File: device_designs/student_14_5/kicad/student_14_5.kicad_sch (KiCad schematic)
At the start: 16 parts

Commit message: feat(family): exact MPNs and hardware design release candidates
Freeze orderable ADLINK COM-HPC-mMTL-155H-32G and Radxa NX5 RM121-D8E32,
verify RM520N-GL Sub-6 with no NTN claim, and deepen five-product EDA/CAD/mfg
packages as honest CANDIDATE releases under PHYSICAL_EXECUTION_FREEZE.

Co-authored-by: Cursor <cursoragent@cursor.com>
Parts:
- UCOM1: value COM-HPC-Mini-Ultra7-155H-32GB -> COM-HPC-mMTL-155H-32G
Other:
- company: gunnchOS3k / HARDWARE FAMILY DEPTH -> gunnchOS3k / HARDWARE DESIGN RELEASE
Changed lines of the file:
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@@
-(kicad_sch (version 20230121) (generator "family_depth_digital")
+(kicad_sch (version 20230121) (generator "hardware_design_release")
   (paper "A3")
   (title_block
     (title "Student 14.5 Carrier — student_14_5_carrier")
     (date "2026-08-08")
-    (rev "0.2.0-dev")
-    (company "gunnchOS3k / HARDWARE FAMILY DEPTH")
+    (rev "0.3.0-dev")
+    (company "gunnchOS3k / HARDWARE DESIGN RELEASE")
     (comment 1 "COM module + carrier — NO bare CPU BGA")
     (comment 2 "ADR-HW-001 / ADR-FP-001")
@@
     (in_bom yes) (on_board yes) (dnp no)
     (property "Reference" "UCOM1" (at 40 33 0) (effects (font (size 1.27 1.27))))
-    (property "Value" "COM-HPC-Mini-Ultra7-155H-32GB" (at 40 47 0) (effects (font (size 1.27 1.27))))
+    (property "Value" "COM-HPC-mMTL-155H-32G" (at 40 47 0) (effects (font (size 1.27 1.27))))
     (property "Footprint" "COM-HPC Mini" (at 40 40 0) (effects (font (size 1.27 1.27)) hide))
     (property "Datasheet" "" (at 40 40 0) (effects (font (size 1.27 1.27)) hide))

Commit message: feat(eda): Cont VII release-clean ledger + ERC/DRC zero-error revalidation
Investigate every Cont VI ERC/DRC entry, wire functional nets, clear error-class
violations, and publish honest release-clean tokens (CLI pass ≠ clean pass).

Co-authored-by: Cursor <cursoragent@cursor.com>
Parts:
- removed BT1: 4S1P_60Wh, pack, symbol Device:R
- removed JCOM1: COM-HPC-Mini-Connector, vendor pair, symbol Device:R
- removed J_EDP: eDP_14_5_panel, FPC, symbol Device:R
- removed J_USB4: USB4_TypeC_x2, USB-C, symbol Device:R
- removed SSD1: NVMe_512GB, M.2 2280, symbol Device:R
- removed UCOM1: COM-HPC-mMTL-155H-32G, COM-HPC Mini, symbol Device:R
- removed U_3V3: TPS62864YCPR, QFN, symbol Device:R
- removed U_5V: TPS51396AJYYR, QFN, symbol Device:R
- removed U_AUD: ALC256, QFN, symbol Device:R
- removed U_CHG: BQ25792RQMR, VQFN, symbol Device:R
- removed U_EC: ITE5570-or-NPCX9, QFP/BGA module, symbol Device:R
- removed U_FG: BQ40Z50-R2, TSSOP, symbol Device:R
- removed U_PD: TPS65994ADFBRQ1, QFN, symbol Device:R
- removed U_TPM: SLB9672XQ2.0, VQFN, symbol Device:R
- removed U_WIFI: BE200, M.2 Key E, symbol Device:R
- removed U_WWAN: RM520N-GL, M.2 3052, symbol Device:R
- added BT1: 4S1P_60Wh, gunnchos_structural:Block_SMD_10x10, symbol FuncBlock
- added JCOM1: COM-HPC-Mini-Connector, gunnchos_structural:Block_SMD_10x10, symbol FuncBlock
- added J_EDP: eDP_14_5_panel, gunnchos_structural:Block_SMD_10x10, symbol FuncBlock
- added J_USB4: USB4_TypeC_x2, gunnchos_structural:Block_SMD_10x10, symbol FuncBlock
- added SSD1: NVMe_512GB, gunnchos_structural:Block_SMD_10x10, symbol FuncBlock
- added UCOM1: COM-HPC-mMTL-155H-32G, gunnchos_structural:Block_SMD_10x10, symbol FuncBlock
- added U_3V3: TPS62864YCPR, gunnchos_structural:Block_SMD_10x10, symbol FuncBlock
- added U_5V: TPS51396AJYYR, gunnchos_structural:Block_SMD_10x10, symbol FuncBlock
- added U_AUD: ALC256, gunnchos_structural:Block_SMD_10x10, symbol FuncBlock
- added U_CHG: BQ25792RQMR, gunnchos_structural:Block_SMD_10x10, symbol FuncBlock
- added U_EC: ITE5570-or-NPCX9, gunnchos_structural:Block_SMD_10x10, symbol FuncBlock
- added U_FG: BQ40Z50-R2, gunnchos_structural:Block_SMD_10x10, symbol FuncBlock
- added U_PD: TPS65994ADFBRQ1, gunnchos_structural:Block_SMD_10x10, symbol FuncBlock
- added U_TPM: SLB9672XQ2.0, gunnchos_structural:Block_SMD_10x10, symbol FuncBlock
- added U_WIFI: BE200, gunnchos_structural:Block_SMD_10x10, symbol FuncBlock
- added U_WWAN: RM520N-GL, gunnchos_structural:Block_SMD_10x10, symbol FuncBlock
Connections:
- net COM_VIN: now also JCOM1.2
- net I2C_EC: now also U_FG.2
- net VBUS_PD: now also U_PD.2
- net VDD_3V3: now also U_EC.2
- net VSYS: now also UCOM1.2
- net eDP0: now also U_CHG.2
- no-connect marks 0 -> 26
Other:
- company: gunnchOS3k / HARDWARE DESIGN RELEASE -> gunnchOS3k / CONTINUATION VII
- title: Student 14.5 Carrier — student_14_5_carrier -> Student 14.5 Carrier — Cont VII

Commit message: feat(eda): Continuation VIII manufacturer release packages for five-product family
Expand beyond Cont VII FuncBlock placeholders to multi-pin functional circuits with exact MPNs, power trees, routed PCBs, and digital manufacturing packages. Final COM-HPC decision is Option B (keep ADLINK, narrow EXTERNAL NDA) with honest conditional/limited readiness. ERC/DRC errors are zero on all five boards under KiCad 10.0.5; PHYSICAL_EXECUTION_FREEZE remains active.

Co-authored-by: Cursor <cursoragent@cursor.com>
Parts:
- removed BT1: 4S1P_60Wh, gunnchos_structural:Block_SMD_10x10, symbol FuncBlock
- removed JCOM1: COM-HPC-Mini-Connector, gunnchos_structural:Block_SMD_10x10, symbol FuncBlock
- removed J_EDP: eDP_14_5_panel, gunnchos_structural:Block_SMD_10x10, symbol FuncBlock
- removed J_USB4: USB4_TypeC_x2, gunnchos_structural:Block_SMD_10x10, symbol FuncBlock
- removed SSD1: NVMe_512GB, gunnchos_structural:Block_SMD_10x10, symbol FuncBlock
- removed UCOM1: COM-HPC-mMTL-155H-32G, gunnchos_structural:Block_SMD_10x10, symbol FuncBlock
- removed U_3V3: TPS62864YCPR, gunnchos_structural:Block_SMD_10x10, symbol FuncBlock
- removed U_5V: TPS51396AJYYR, gunnchos_structural:Block_SMD_10x10, symbol FuncBlock
- removed U_AUD: ALC256, gunnchos_structural:Block_SMD_10x10, symbol FuncBlock
- removed U_CHG: BQ25792RQMR, gunnchos_structural:Block_SMD_10x10, symbol FuncBlock
- removed U_EC: ITE5570-or-NPCX9, gunnchos_structural:Block_SMD_10x10, symbol FuncBlock
- removed U_FG: BQ40Z50-R2, gunnchos_structural:Block_SMD_10x10, symbol FuncBlock
- removed U_PD: TPS65994ADFBRQ1, gunnchos_structural:Block_SMD_10x10, symbol FuncBlock
- removed U_TPM: SLB9672XQ2.0, gunnchos_structural:Block_SMD_10x10, symbol FuncBlock
- removed U_WIFI: BE200, gunnchos_structural:Block_SMD_10x10, symbol FuncBlock
- removed U_WWAN: RM520N-GL, gunnchos_structural:Block_SMD_10x10, symbol FuncBlock
- added C1: CL05A104KA5NNNC, gunnchos_functional:C_0402, symbol C
- added C2: GRM188R60J106ME47D, gunnchos_functional:C_0402, symbol C
- added D1: APTD1608LCGCK, gunnchos_functional:LED_0603, symbol LED
- added DESD1: PESD5V0S1UL, gunnchos_functional:R_0402, symbol C
- added JDISP1: eDP_primary_panel, gunnchos_functional:Block_SMD_safe, symbol PANEL_EDP
- added JUSB1: TYPE-C-31-M-12, gunnchos_functional:Block_SMD_safe, symbol USB_C
- added R1: RC0402FR-0710KL, gunnchos_functional:R_0402, symbol R
- added R2: RC0402FR-071K0L, gunnchos_functional:R_0402, symbol R
- added U3V3: TPS62864, gunnchos_functional:Block_SMD_safe, symbol BUCK
- added UCHG1: BQ25792RQMR, gunnchos_functional:Block_SMD_safe, symbol CHARGER
- added UCOM1: COM-HPC-mMTL-155H-32G, gunnchos_functional:Block_SMD_safe, symbol COMHPC_PUBLIC
- added UPD1: TPS65994ADFBRQ1, gunnchos_functional:Block_SMD_safe, symbol PD_CTRL
- added UTPM1: SLB9672XQ2.0, gunnchos_functional:Block_SMD_safe, symbol TPM
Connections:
- net COM_VIN: now also UCOM1.PWRBTN
- net VDD_3V3: now also C1.1, JDISP1.7 (T_SCL), R1.1, R2.1, U3V3.2 (EN), U3V3.4 (VOUT), UPD1.2 (CC1), UTPM1.5 (SPI_MOSI)
- net VSYS: now also C2.1, U3V3.3 (GND), UCHG1.6 (SDA), UPD1.1 (VBUS)
- new net BL_EN: JDISP1.3 (EDP_TX0N)
- new net BL_PWM: JDISP1.4 (EDP_TX0P)
- new net CC1: DESD1.1, JUSB1.A5 (CC1), UPD1.8 (3V3)
- new net EDP0_N: JDISP1.5 (BL_EN)
- new net EDP0_P: JDISP1.6 (BL_PWM)
- new net GND: C1.2, C2.2, D1.1 (K), DESD1.2, JDISP1.8 (T_SDA), JUSB1.A7 (DM), U3V3.1 (VIN), UCHG1.4 (GND), UCOM1.UART_TX, UPD1.6 (SDA), UTPM1.6 (SPI_MISO)
- new net I2C_SCL: JDISP1.1 (VDD), R1.2, UCHG1.1 (VBUS), UPD1.3 (CC2)
- new net I2C_SDA: JDISP1.2 (GND), UCHG1.2 (SYS), UPD1.4 (GND)
- new net LED_A: D1.2 (A), R2.2
- new net PWRBTN: UCOM1.VIN (VIN_12V)
- new net SPI_CLK: UTPM1.4 (SPI_CLK)
- new net SPI_CS: UTPM1.3 (SPI_CS)
- new net SPI_MISO: UTPM1.2 (GND)
- new net SPI_MOSI: UTPM1.1 (VDD)
- new net UART_TX: UCOM1.GND
- new net VBAT: UCHG1.3 (BAT)
- new net VBUS: JUSB1.B5 (CC2), UCHG1.5 (SCL), UPD1.7 (VSYS)
- no-connect marks 26 -> 4
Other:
- note added: "Cont VIII functional schematic — multi-pin symbols + exact MPNs (not FuncBlock placeholders)."
- note added: "EXTERNAL_NDA_BLOCKED: COM-HPC Mini 400-pin net-accurate map"
- note added: "Revision 0.5.0-cont-viii."
- note added: "SI notes encoded on PCB stackup/Dwgs — no SI simulation claimed."
- company: gunnchOS3k / CONTINUATION VII -> gunnchOS3k / CONTINUATION VIII
- title: Student 14.5 Carrier — Cont VII -> Student 14.5 Carrier — Cont VIII Option B

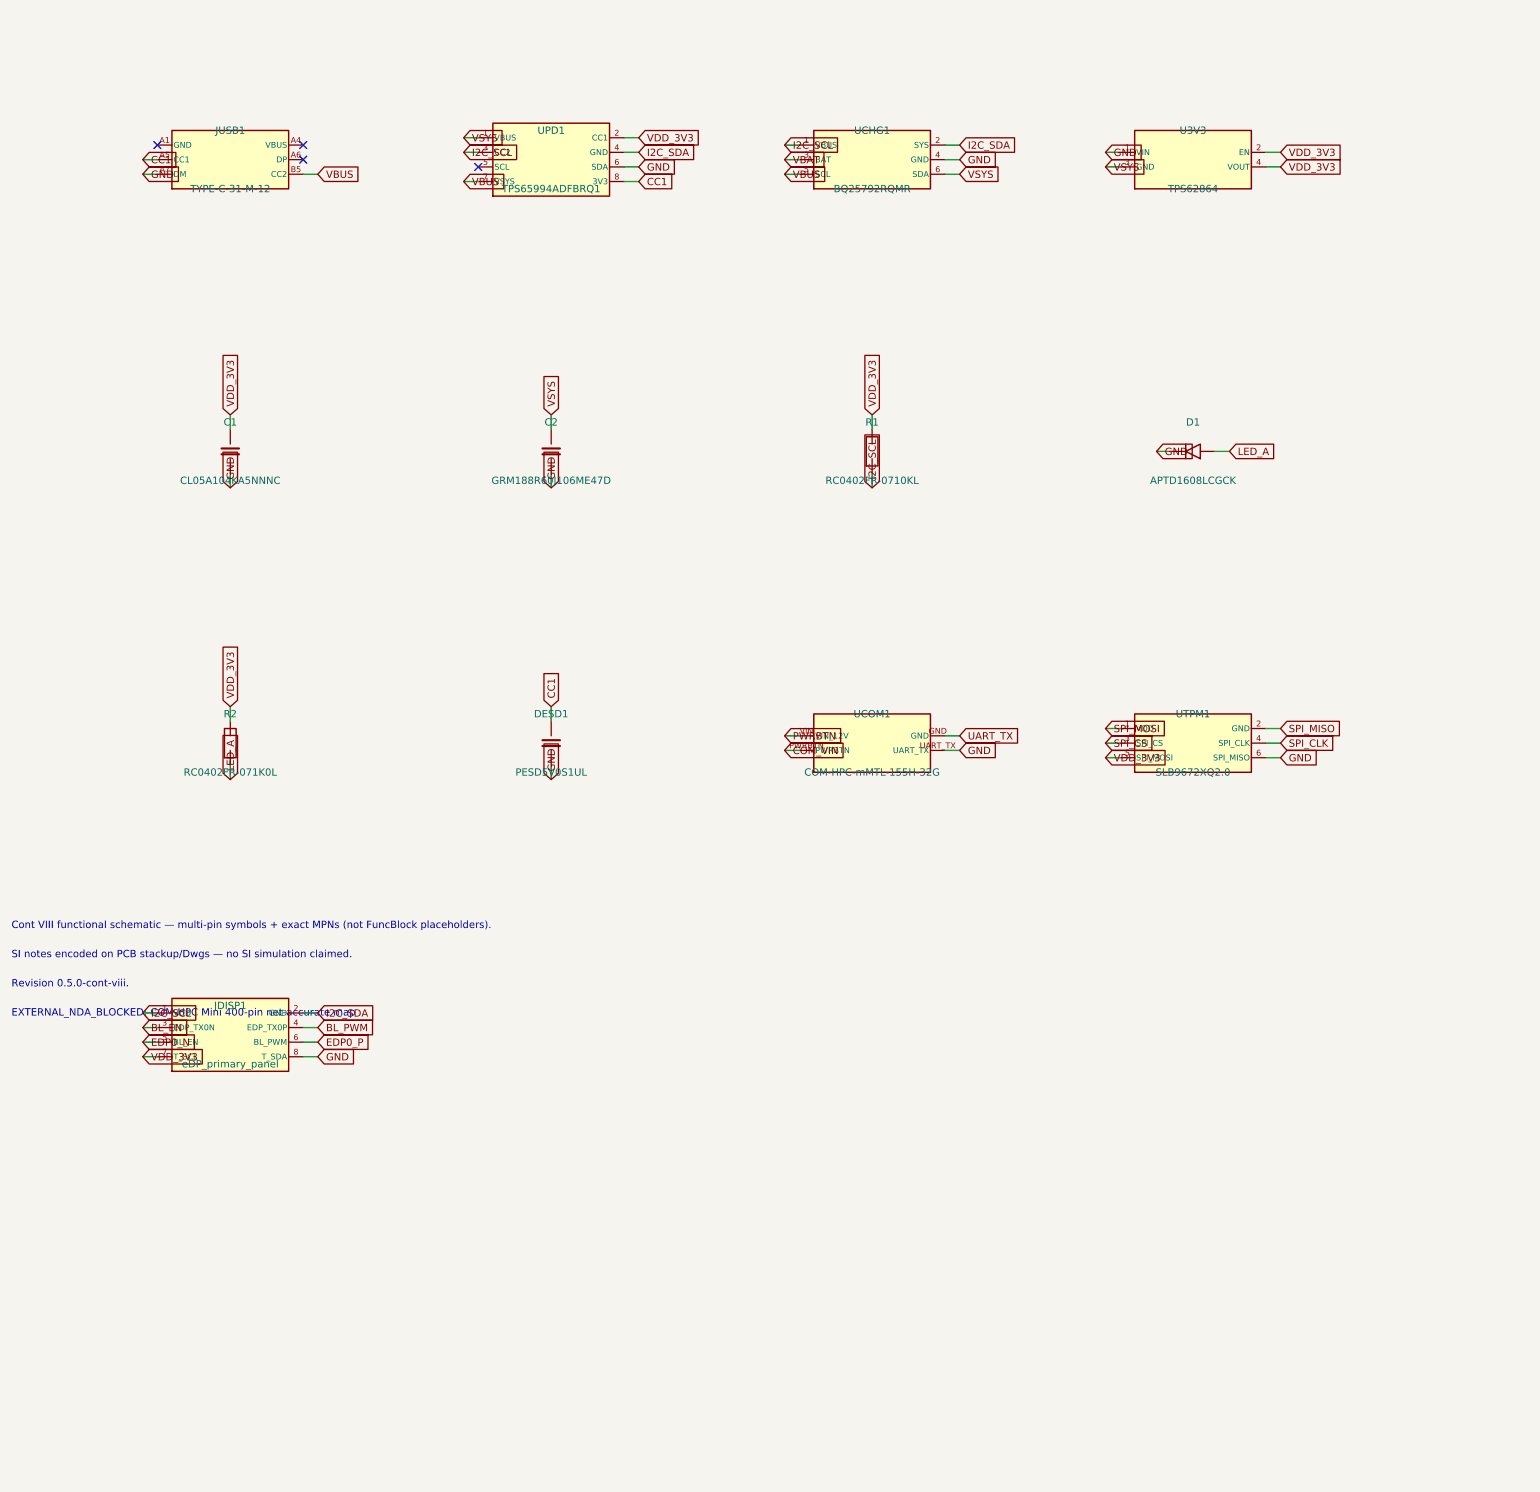
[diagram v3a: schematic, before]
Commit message: feat(eda): Continuation IX Pre-EVT digital release lock for five-product family
Close Cont VIII residual DIGITAL blockers with production footprints, full Radxa 260-pin hierarchical sheets, assembly/RFQ/EVT packages, and honest ADLINK-retained COM-HPC tokens under PHYSICAL_EXECUTION_FREEZE.

Co-authored-by: Cursor <cursoragent@cursor.com>
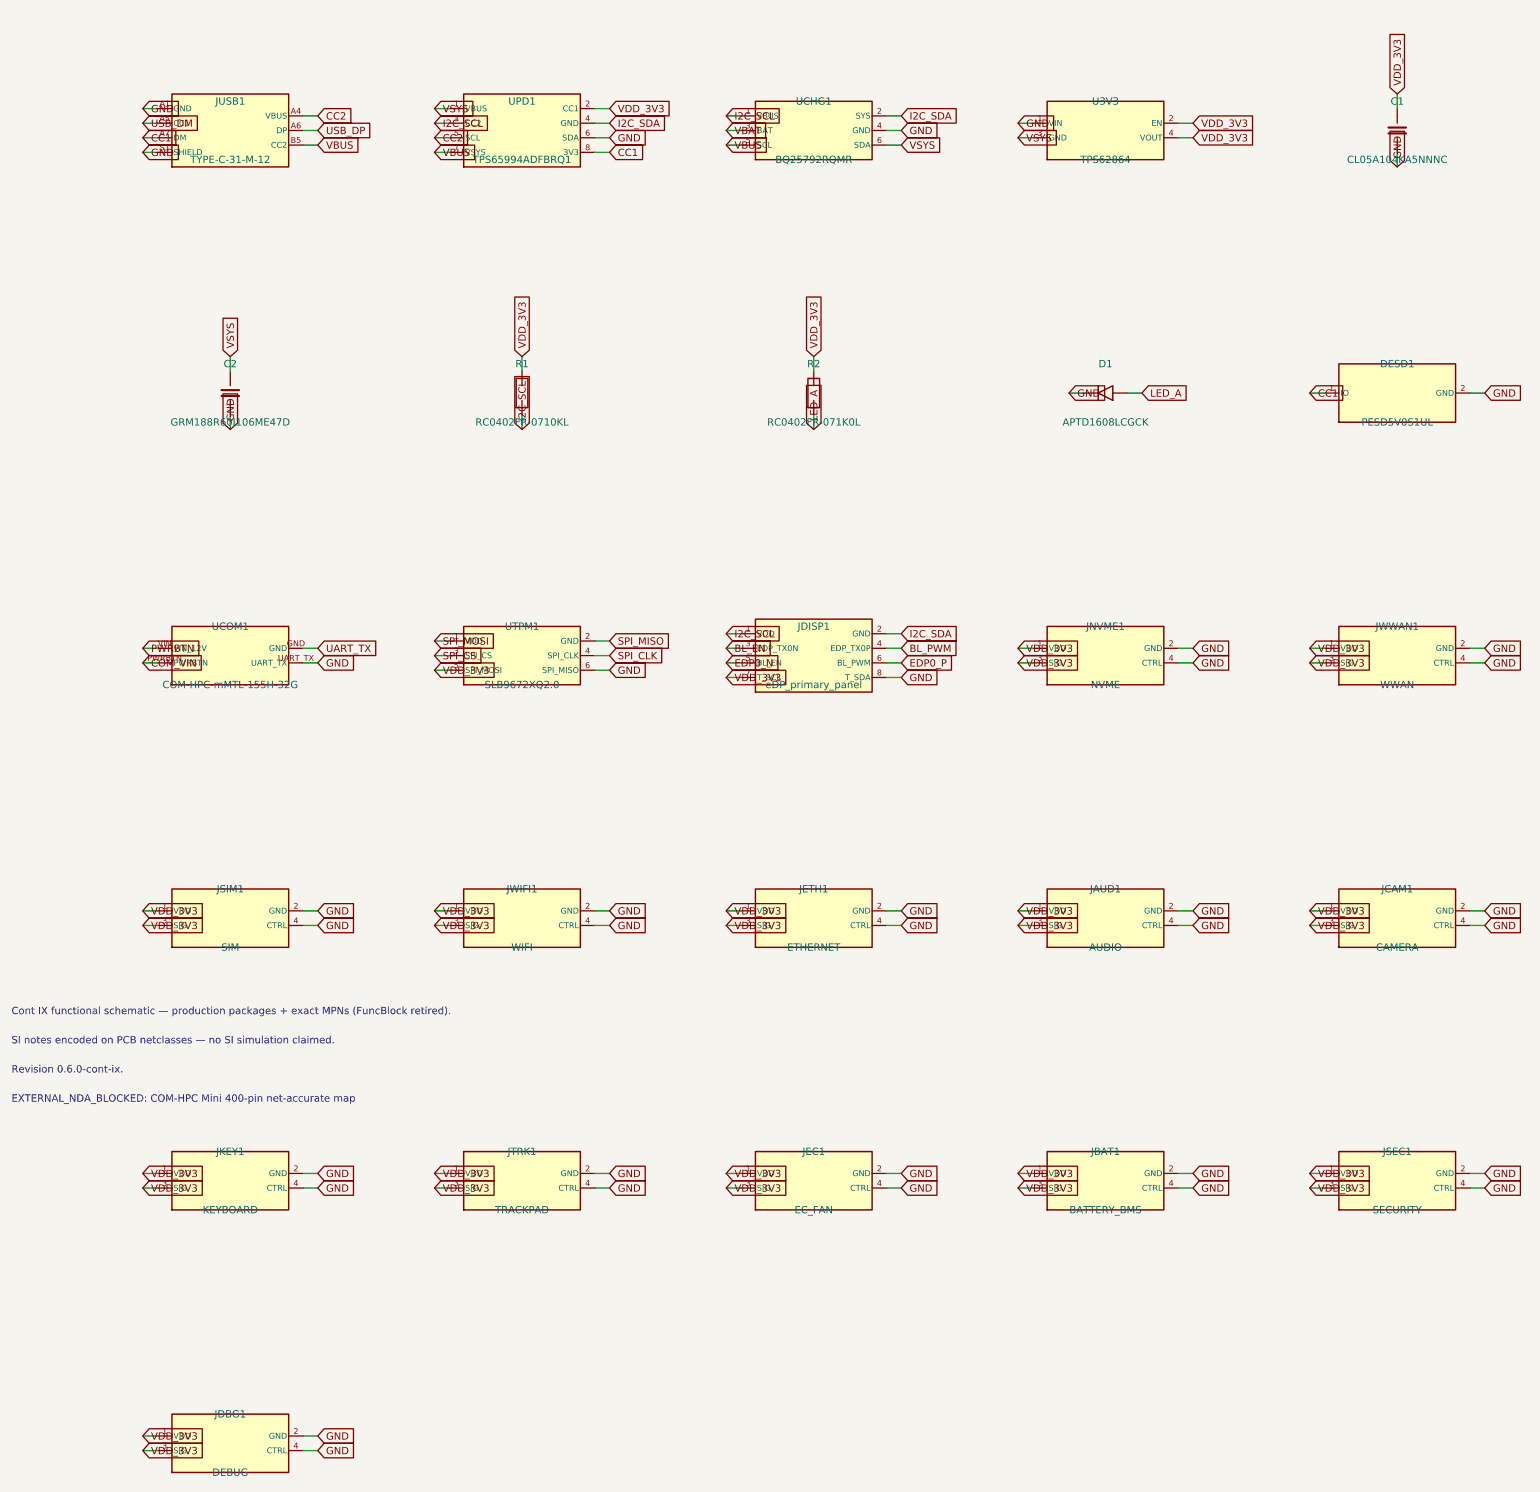
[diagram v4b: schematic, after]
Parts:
- added JAUD1: AUDIO, gunnchos_production:DFN1006-2, symbol PERIPH
- added JBAT1: BATTERY_BMS, gunnchos_production:DFN1006-2, symbol PERIPH
- added JCAM1: CAMERA, gunnchos_production:FFC_40P_0.5mm, symbol PERIPH
- added JDBG1: DEBUG, gunnchos_production:DFN1006-2, symbol PERIPH
- added JEC1: EC_FAN, gunnchos_production:DFN1006-2, symbol PERIPH
- added JETH1: ETHERNET, gunnchos_production:DFN1006-2, symbol PERIPH
- added JKEY1: KEYBOARD, gunnchos_production:DFN1006-2, symbol PERIPH
- added JNVME1: NVME, gunnchos_production:FFC_40P_0.5mm, symbol PERIPH
- added JSEC1: SECURITY, gunnchos_production:DFN1006-2, symbol PERIPH
- added JSIM1: SIM, gunnchos_production:DFN1006-2, symbol PERIPH
- added JTRK1: TRACKPAD, gunnchos_production:DFN1006-2, symbol PERIPH
- added JWIFI1: WIFI, gunnchos_production:DFN1006-2, symbol PERIPH
- added JWWAN1: WWAN, gunnchos_production:FFC_40P_0.5mm, symbol PERIPH
- C1, C2: footprint gunnchos_functional:C_0402 -> gunnchos_production:C_0402; ContIX (none) -> PRODUCTION; ContVIII FUNCTIONAL -> (none)
- D1: footprint gunnchos_functional:LED_0603 -> gunnchos_production:LED_0603; ContIX (none) -> PRODUCTION; ContVIII FUNCTIONAL -> (none)
- DESD1: footprint gunnchos_functional:R_0402 -> gunnchos_production:DFN1006-2; symbol C -> ESD; ContIX (none) -> PRODUCTION; ContVIII FUNCTIONAL -> (none)
- JDISP1: footprint gunnchos_functional:Block_SMD_safe -> gunnchos_production:FFC_40P_0.5mm; ContIX (none) -> PRODUCTION; ContVIII FUNCTIONAL -> (none)
- JUSB1: footprint gunnchos_functional:Block_SMD_safe -> gunnchos_production:USB_C_Receptacle_Production; ContIX (none) -> PRODUCTION; ContVIII FUNCTIONAL -> (none)
- R1, R2: footprint gunnchos_functional:R_0402 -> gunnchos_production:R_0402; ContIX (none) -> PRODUCTION; ContVIII FUNCTIONAL -> (none)
- U3V3: footprint gunnchos_functional:Block_SMD_safe -> gunnchos_production:QFN-16-1EP_3x3mm_P0.5mm; ContIX (none) -> PRODUCTION; ContVIII FUNCTIONAL -> (none)
- UCHG1: footprint gunnchos_functional:Block_SMD_safe -> gunnchos_production:WQFN-29-1EP_4x4mm_P0.4mm; ContIX (none) -> PRODUCTION; ContVIII FUNCTIONAL -> (none)
- UCOM1: footprint gunnchos_functional:Block_SMD_safe -> gunnchos_production:COMHPC_Mini_envelope; ContIX (none) -> PRODUCTION; ContVIII FUNCTIONAL -> (none)
- UPD1: footprint gunnchos_functional:Block_SMD_safe -> gunnchos_production:VQFN-48-1EP_7x7mm_P0.5mm; ContIX (none) -> PRODUCTION; ContVIII FUNCTIONAL -> (none)
- UTPM1: footprint gunnchos_functional:Block_SMD_safe -> gunnchos_production:VQFN-32-1EP_5x5mm_P0.5mm; ContIX (none) -> PRODUCTION; ContVIII FUNCTIONAL -> (none)
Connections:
- net CC1: now also JUSB1.A7 (DM); no longer JUSB1.A5 (CC1)
- net GND: now also JUSB1.A1 (GND), JUSB1.S1 (SHIELD), JAUD1.2 (GND), JAUD1.4 (CTRL), JBAT1.2 (GND), JBAT1.4 (CTRL), JCAM1.2 (GND), JCAM1.4 (CTRL), JDBG1.2 (GND), JDBG1.4 (CTRL), JEC1.2 (GND), JEC1.4 (CTRL), JETH1.2 (GND), JETH1.4 (CTRL), JKEY1.2 (GND), JKEY1.4 (CTRL), JNVME1.2 (GND), JNVME1.4 (CTRL), JSEC1.2 (GND), JSEC1.4 (CTRL), JSIM1.2 (GND), JSIM1.4 (CTRL), JTRK1.2 (GND), JTRK1.4 (CTRL), JWIFI1.2 (GND), JWIFI1.4 (CTRL), JWWAN1.2 (GND), JWWAN1.4 (CTRL); no longer JUSB1.A7 (DM)
- net VDD_3V3: now also JAUD1.1 (VDD), JAUD1.3 (SIG), JBAT1.1 (VDD), JBAT1.3 (SIG), JCAM1.1 (VDD), JCAM1.3 (SIG), JDBG1.1 (VDD), JDBG1.3 (SIG), JEC1.1 (VDD), JEC1.3 (SIG), JETH1.1 (VDD), JETH1.3 (SIG), JKEY1.1 (VDD), JKEY1.3 (SIG), JNVME1.1 (VDD), JNVME1.3 (SIG), JSEC1.1 (VDD), JSEC1.3 (SIG), JSIM1.1 (VDD), JSIM1.3 (SIG), JTRK1.1 (VDD), JTRK1.3 (SIG), JWIFI1.1 (VDD), JWIFI1.3 (SIG), JWWAN1.1 (VDD), JWWAN1.3 (SIG)
- net CC2: now reaches UPD1.5 (SCL)
- net CC2: now also JUSB1.A4 (VBUS)
- net USB_DP: now reaches JUSB1.A6 (DP)
- new net USB_DM: JUSB1.A5 (CC1)
- no-connect marks 4 -> 0
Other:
- note added: "Cont IX functional schematic — production packages + exact MPNs (FuncBlock retired)."
- note added: "Revision 0.6.0-cont-ix."
- note added: "SI notes encoded on PCB netclasses — no SI simulation claimed."
- note removed: "Cont VIII functional schematic — multi-pin symbols + exact MPNs (not FuncBlock placeholders)."
- note removed: "Revision 0.5.0-cont-viii."
- note removed: "SI notes encoded on PCB stackup/Dwgs — no SI simulation claimed."
- company: gunnchOS3k / CONTINUATION VIII -> gunnchOS3k / CONTINUATION IX
- title: Student 14.5 Carrier — Cont VIII Option B -> Student 14.5 Carrier — Cont IX Option B ADLINK
- moved on the sheet: C1, C2, D1, JDISP1, R1, R2, U3V3, UCHG1, UCOM1, UPD1, UTPM1
